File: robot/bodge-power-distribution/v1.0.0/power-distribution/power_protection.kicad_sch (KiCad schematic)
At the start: 34 parts

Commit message: Incomplete bodge-power-distribution schematics
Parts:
- removed R?: 10k, Resistor_SMD:R_0402_1005Metric_Pad0.72x0.64mm_HandSolder, symbol Device:R_Small_US
- added F?: TBD_MASTER_FUSE, symbol Device:Fuse
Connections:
- net V_{BATT}: now also F?.1; no longer Q?.3 (D), R?.1, U?.1 (V_{in})
- net FAULT_{OD} renamed ~{FAULT}
- net TEMP_MON_{pwr}_1v25 renamed TEMP_MON_{PWR(1v25)}
- net TempMon_{pwr} renamed TempMon_{PWR}
- new net: F?.2, Q?.3 (D), R?.1, U?.1 (V_{IN})
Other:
- note added: "Up to 80V"
- note removed: "up to 80V"
- title: Motorboard -> Power Distribution

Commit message: Incomplete bodge-power-distribution schematics
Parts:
- removed Q? (x2): SQJA80EP-T1_GE3, Package_TO_SOT_SMD:Vishay_PowerPAK_SC70-6L_Single, symbol Device:Q_NMOS_SGD
- removed R?: 69.8k, Resistor_SMD:R_0402_1005Metric_Pad0.72x0.64mm_HandSolder, symbol Device:R_Small_US
- removed R?: 115k, Resistor_SMD:R_0402_1005Metric_Pad0.72x0.64mm_HandSolder, symbol Device:R_Small_US
- added Q1, Q2: SQJA80EP-T1_GE3, Package_SO:PowerPAK_SO-8_Single, symbol transistors:Q_NMOS_SGD_PowerPAK
- added R4, R5: 39k, Resistor_SMD:R_0402_1005Metric_Pad0.72x0.64mm_HandSolder, symbol Device:R_Small_US
- gave numbers to parts that had none: 30
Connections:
- net GND: now also R4.2, R5.2
- net V_{BATT(PROTECTED)}: now also Q2.5 (D)
- net at F1.2, R6.1, U2.1 (V_{IN}): now also Q1.5 (D)
- net at R20.1: now also Q1.4 (G)
- net at U1.7 (CH6): now also R5.1
- net at U1.8 (CH7): now also R4.1
- net at R23.2: now also Q2.4 (G)
- new net: Q1.1 (S), Q1.2 (S), Q1.3 (S), Q2.1 (S), Q2.2 (S), Q2.3 (S)
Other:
- note added: "80V Tolerant"
- note removed: "Power Regulator Temperature Monitor Voltage Divider"
- note removed: "Up to 80V"
- moved on the sheet: C4, C5, C6, C7, F1, R10, R11, R12, R13, R14, R15, R16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

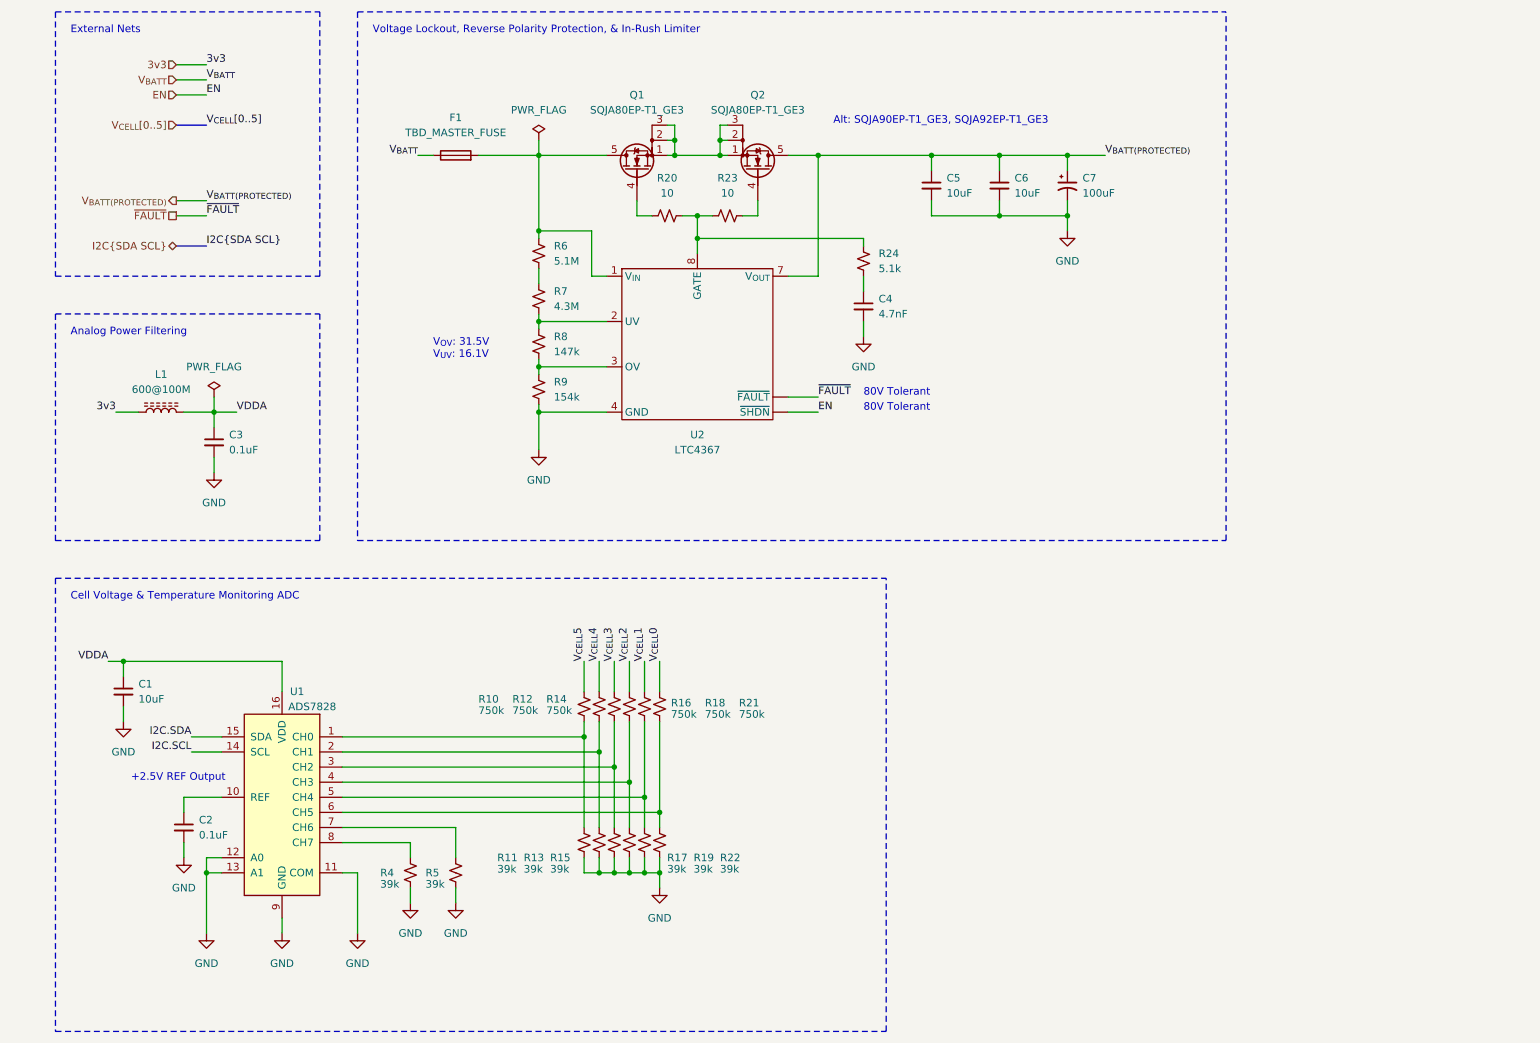
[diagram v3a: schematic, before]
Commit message: Separated power monitor into its own sheet
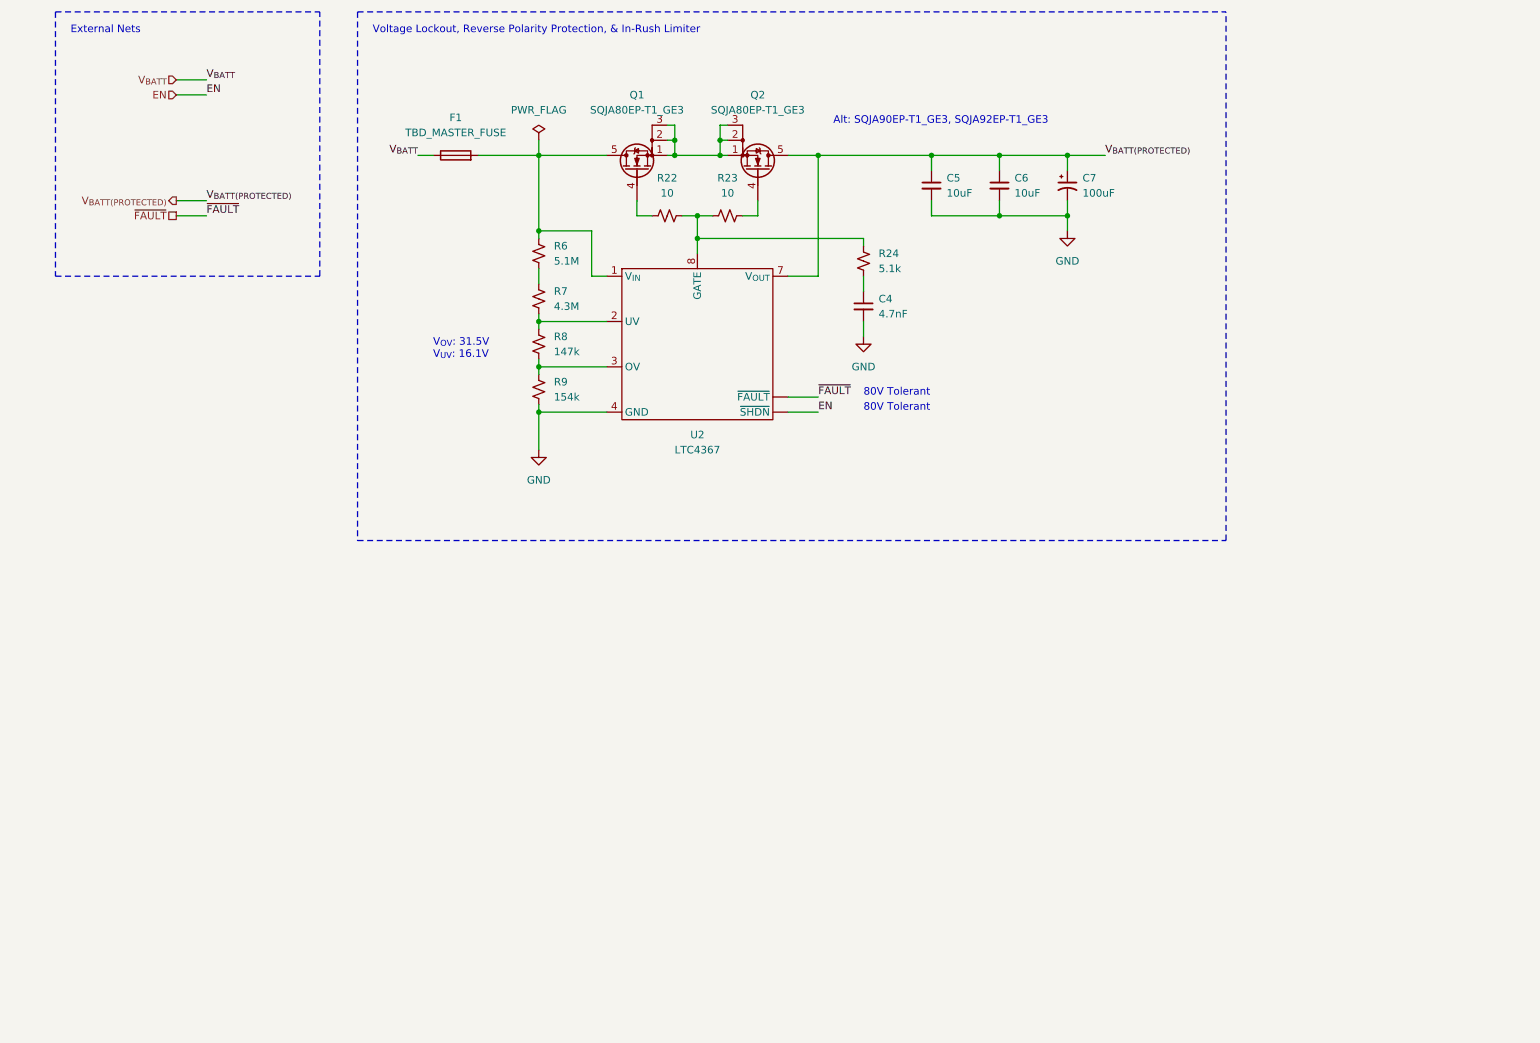
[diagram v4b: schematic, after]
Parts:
- removed C1: 10uF, Capacitor_SMD:C_1210_3225Metric_Pad1.33x2.70mm_HandSolder, symbol Device:C_Small
- removed C2, C3: 0.1uF, Capacitor_SMD:C_0402_1005Metric_Pad0.74x0.62mm_HandSolder, symbol Device:C_Small
- removed L1: 600@100M, Inductor_SMD:L_0603_1608Metric_Pad1.05x0.95mm_HandSolder, symbol Device:L_Ferrite
- removed R10, R12, R14, R16, R18, R21: 750k, Resistor_SMD:R_0402_1005Metric_Pad0.72x0.64mm_HandSolder, symbol Device:R_Small_US
- removed R11, R13, R15, R17, R19, R22, R4, R5: 39k, Resistor_SMD:R_0402_1005Metric_Pad0.72x0.64mm_HandSolder, symbol Device:R_Small_US
- removed U1: ADS7828, Package_SO:TSSOP-16_4.4x5mm_P0.65mm, symbol Analog_ADC:ADS7828
- renumbered R20 to R22
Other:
- note removed: "+2.5V REF Output"
- note removed: "Analog Power Filtering"
- note removed: "Cell Voltage & Temperature Monitoring ADC"

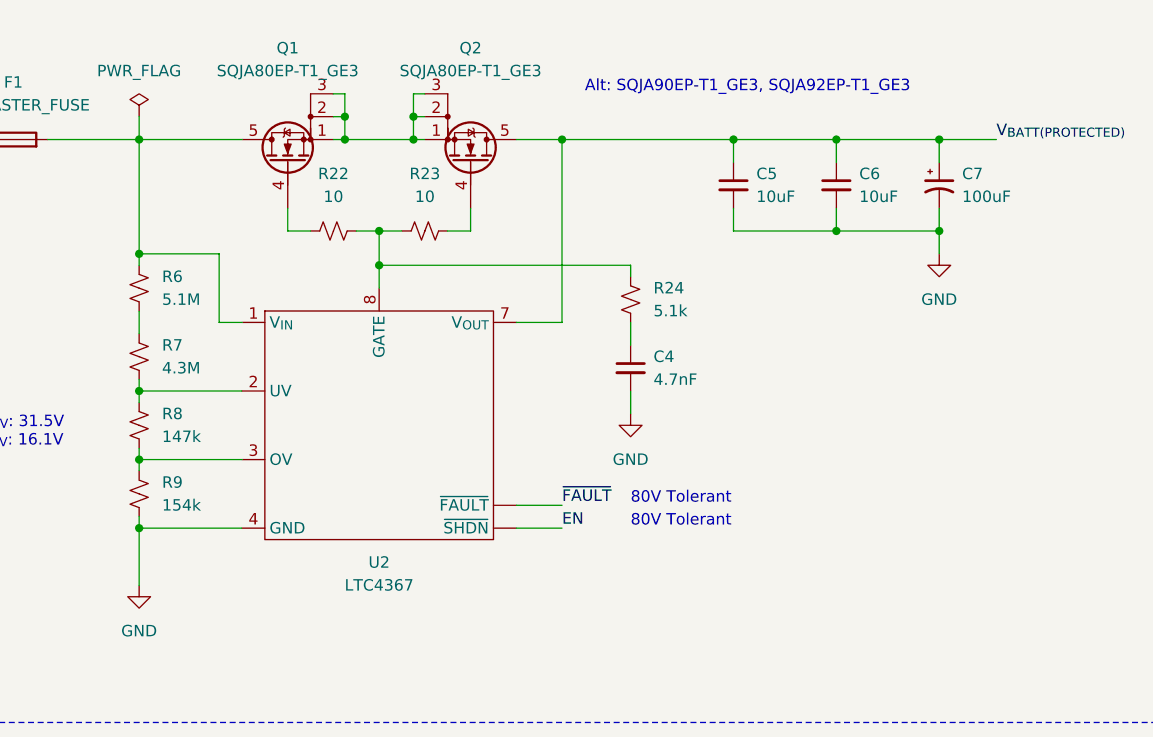
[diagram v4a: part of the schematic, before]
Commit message: Rename transistors library to AT-Transistors
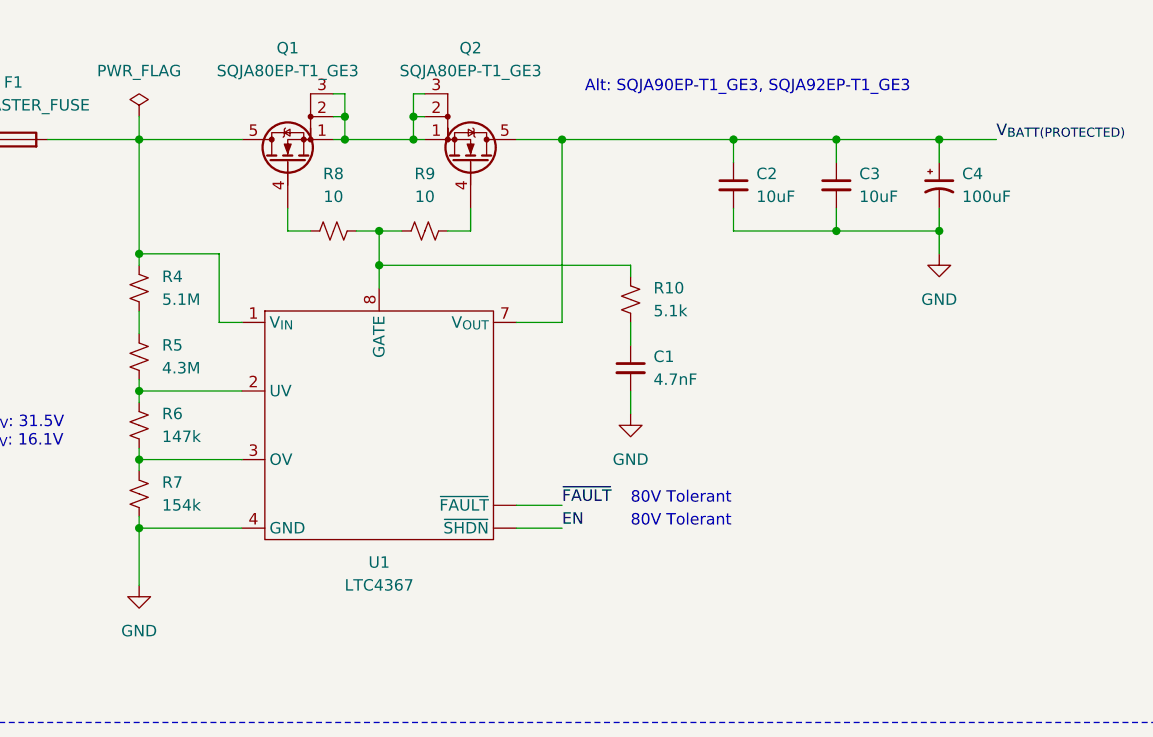
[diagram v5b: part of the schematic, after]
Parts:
- removed Q1: SQJA80EP-T1_GE3, Package_SO:PowerPAK_SO-8_Single, symbol transistors:Q_NMOS_SGD_PowerPAK
- added Q1: SQJA80EP-T1_GE3, Package_SO:PowerPAK_SO-8_Single, symbol AT-Transistors:Q_NMOS_SGD_PowerPAK
- Q2: symbol transistors:Q_NMOS_SGD_PowerPAK -> AT-Transistors:Q_NMOS_SGD_PowerPAK
- renumbered C4 to C1, C5 to C2, C6 to C3, C7 to C4, R24 to R10, R6 to R4, R7 to R5, R8 to R6, R9 to R7, R22 to R8, R23 to R9, U2 to U1
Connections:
- net at F1.2, R4.1, U1.1 (V_{IN}): now also Q1.5 (D)
- net at Q2.1 (S), Q2.2 (S), Q2.3 (S): now also Q1.1 (S), Q1.2 (S), Q1.3 (S)
- net at R8.1: now also Q1.4 (G)
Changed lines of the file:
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@@
   (symbol (lib_id "Device:R_Small_US") (at 100.33 59.69 0) (unit 1)
     (in_bom yes) (on_board yes) (fields_autoplaced)
-    (property "Reference" "R6" (id 0) (at 102.87 58.4199 0)
+    (property "Reference" "R4" (id 0) (at 102.87 58.4199 0)
       (effects (font (size 1.27 1.27)) (justify left))
     )
@@
     (pin "2")
   )
-  (symbol (lib_id "transistors:Q_NMOS_SGD_PowerPAK") (at 137.16 45.72 270) (mirror x) (unit 1)
+  (symbol (lib_id "AT-Transistors:Q_NMOS_SGD_PowerPAK") (at 137.16 45.72 270) (mirror x) (unit 1)
     (in_bom yes) (on_board yes)
     (property "Reference" "Q2" (id 0) (at 137.16 33.02 90))
@@
   (symbol (lib_id "Device:R_Small_US") (at 100.33 67.31 0) (unit 1)
     (in_bom yes) (on_board yes) (fields_autoplaced)
-    (property "Reference" "R7" (id 0) (at 102.87 66.0399 0)
+    (property "Reference" "R5" (id 0) (at 102.87 66.0399 0)
       (effects (font (size 1.27 1.27)) (justify left))
     )
@@
     (pin "2")
   )
+  (symbol (lib_id "AT-Transistors:Q_NMOS_SGD_PowerPAK") (at 116.84 45.72 90) (unit 1)
+    (in_bom yes) (on_board yes)
+    (property "Reference" "Q1" (id 0) (at 116.84 33.02 90))
+    (property "Value" "SQJA80EP-T1_GE3" (id 1) (at 116.84 35.56 90))
+    (property "Footprint" "Package_SO:PowerPAK_SO-8_Single" (id 2) (at 114.3 40.64 0)
+      (effects (font (size 1.27 1.27)) hide)
+    )
+    (property "Datasheet" "~" (id 3) (at 116.84 45.72 0)
+      (effects (font (size 1.27 1.27)) hide)
+    )
+    (pin "1")
+    (pin "2")
+    (pin "3")
+    (pin "4")
+    (pin "5")
+  )
   (symbol (lib_id "Device:C_Polarized_Small_US") (at 189.23 48.26 0) (unit 1)
     (in_bom yes) (on_board yes) (fields_autoplaced)
-    (property "Reference" "C7" (id 0) (at 191.77 46.9899 0)
+    (property "Reference" "C4" (id 0) (at 191.77 46.9899 0)
       (effects (font (size 1.27 1.27)) (justify left))
     )
@@
   (symbol (lib_id "Device:R_Small_US") (at 154.94 60.96 0) (unit 1)
     (in_bom yes) (on_board yes) (fields_autoplaced)
-    (property "Reference" "R24" (id 0) (at 157.48 59.6899 0)
+    (property "Reference" "R10" (id 0) (at 157.48 59.6899 0)
       (effects (font (size 1.27 1.27)) (justify left))
     )
@@
   (symbol (lib_id "power:GND") (at 154.94 73.66 0) (unit 1)
     (in_bom yes) (on_board yes) (fields_autoplaced)
-    (property "Reference" "#PWR022" (id 0) (at 154.94 80.01 0)
+    (property "Reference" "#PWR012" (id 0) (at 154.94 80.01 0)
       (effects (font (size 1.27 1.27)) hide)
     )
@@
   (symbol (lib_id "ltc_regulators:LTC4367") (at 127 74.93 0) (unit 1)
     (in_bom yes) (on_board yes) (fields_autoplaced)
-    (property "Reference" "U2" (id 0) (at 127 90.17 0))
+    (property "Reference" "U1" (id 0) (at 127 90.17 0))
     (property "Value" "LTC4367" (id 1) (at 127 92.71 0))
     (property "Footprint" "" (id 2) (at 127 74.93 0)
@@
   (symbol (lib_id "power:PWR_FLAG") (at 100.33 40.64 0) (unit 1)
     (in_bom yes) (on_board yes) (fields_autoplaced)
-    (property "Reference" "#FLG04" (id 0) (at 100.33 38.735 0)
+    (property "Reference" "#FLG03" (id 0) (at 100.33 38.735 0)
       (effects (font (size 1.27 1.27)) hide)
     )
@@
   (symbol (lib_id "power:GND") (at 189.23 55.88 0) (unit 1)
     (in_bom yes) (on_board yes) (fields_autoplaced)
-    (property "Reference" "#PWR023" (id 0) (at 189.23 62.23 0)
+    (property "Reference" "#PWR013" (id 0) (at 189.23 62.23 0)
       (effects (font (size 1.27 1.27)) hide)
     )
@@
   (symbol (lib_id "Device:C_Small") (at 166.37 48.26 0) (unit 1)
     (in_bom yes) (on_board yes) (fields_autoplaced)
-    (property "Reference" "C5" (id 0) (at 168.91 46.9899 0)
+    (property "Reference" "C2" (id 0) (at 168.91 46.9899 0)
       (effects (font (size 1.27 1.27)) (justify left))
     )
@@
   (symbol (lib_id "Device:C_Small") (at 177.8 48.26 0) (unit 1)
     (in_bom yes) (on_board yes) (fields_autoplaced)
-    (property "Reference" "C6" (id 0) (at 180.34 46.9899 0)
+    (property "Reference" "C3" (id 0) (at 180.34 46.9899 0)
       (effects (font (size 1.27 1.27)) (justify left))
     )
@@
   (symbol (lib_id "Device:R_Small_US") (at 132.08 53.34 90) (unit 1)
     (in_bom yes) (on_board yes) (fields_autoplaced)
-    (property "Reference" "R23" (id 0) (at 132.08 46.99 90))
+    (property "Reference" "R9" (id 0) (at 132.08 46.99 90))
     (property "Value" "10" (id 1) (at 132.08 49.53 90))
     (property "Footprint" "Resistor_SMD:R_0402_1005Metric_Pad0.72x0.64mm_HandSolder" (id 2) (at 132.08 53.34 0)
@@
   (symbol (lib_id "Device:C_Small") (at 154.94 68.58 0) (unit 1)
     (in_bom yes) (on_board yes) (fields_autoplaced)
-    (property "Reference" "C4" (id 0) (at 157.48 67.3099 0)
+    (property "Reference" "C1" (id 0) (at 157.48 67.3099 0)
       (effects (font (size 1.27 1.27)) (justify left))
     )
@@
   (symbol (lib_id "power:GND") (at 100.33 92.71 0) (unit 1)
     (in_bom yes) (on_board yes)
-    (property "Reference" "#PWR020" (id 0) (at 100.33 99.06 0)
+    (property "Reference" "#PWR011" (id 0) (at 100.33 99.06 0)
       (effects (font (size 1.27 1.27)) hide)
     )
@@
   (symbol (lib_id "Device:R_Small_US") (at 100.33 74.93 0) (unit 1)
     (in_bom yes) (on_board yes) (fields_autoplaced)
-    (property "Reference" "R8" (id 0) (at 102.87 73.6599 0)
+    (property "Reference" "R6" (id 0) (at 102.87 73.6599 0)
       (effects (font (size 1.27 1.27)) (justify left))
     )
@@
   (symbol (lib_id "Device:R_Small_US") (at 121.92 53.34 90) (unit 1)
     (in_bom yes) (on_board yes) (fields_autoplaced)
-    (property "Reference" "R22" (id 0) (at 121.92 46.99 90))
+    (property "Reference" "R8" (id 0) (at 121.92 46.99 90))
     (property "Value" "10" (id 1) (at 121.92 49.53 90))
     (property "Footprint" "Resistor_SMD:R_0402_1005Metric_Pad0.72x0.64mm_HandSolder" (id 2) (at 121.92 53.34 0)
@@
   (symbol (lib_id "Device:R_Small_US") (at 100.33 82.55 180) (unit 1)
     (in_bom yes) (on_board yes) (fields_autoplaced)
-    (property "Reference" "R9" (id 0) (at 102.87 81.2799 0)
+    (property "Reference" "R7" (id 0) (at 102.87 81.2799 0)
       (effects (font (size 1.27 1.27)) (justify right))
     )
@@
     (pin "2")
   )
-  (symbol (lib_id "transistors:Q_NMOS_SGD_PowerPAK") (at 116.84 45.72 90) (unit 1)
-    (in_bom yes) (on_board yes)
-    (property "Reference" "Q1" (id 0) (at 116.84 33.02 90))
-    (property "Value" "SQJA80EP-T1_GE3" (id 1) (at 116.84 35.56 90))
-    (property "Footprint" "Package_SO:PowerPAK_SO-8_Single" (id 2) (at 114.3 40.64 0)
-      (effects (font (size 1.27 1.27)) hide)
-    )
-    (property "Datasheet" "~" (id 3) (at 116.84 45.72 0)
-      (effects (font (size 1.27 1.27)) hide)
-    )
-    (pin "1")
-    (pin "2")
-    (pin "3")
-    (pin "4")
-    (pin "5")
-  )
 )

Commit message: Component updates
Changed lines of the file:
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@@
     (stroke (width 0) (type solid) (color 0 0 0 0))
   )
-  (wire (pts (xy 100.33 86.36) (xy 100.33 92.71))
+  (wire (pts (xy 100.33 86.36) (xy 100.33 87.63))
     (stroke (width 0) (type solid) (color 0 0 0 0))
   )
@@
     (pin "2")
   )
-  (symbol (lib_id "power:GND") (at 100.33 92.71 0) (unit 1)
+  (symbol (lib_id "power:GND") (at 100.33 87.63 0) (unit 1)
     (in_bom yes) (on_board yes)
-    (property "Reference" "#PWR011" (id 0) (at 100.33 99.06 0)
-      (effects (font (size 1.27 1.27)) hide)
-    )
-    (property "Value" "GND" (id 1) (at 100.33 97.79 0))
-    (property "Footprint" "" (id 2) (at 100.33 92.71 0)
-      (effects (font (size 1.27 1.27)) hide)
-    )
-    (property "Datasheet" "" (id 3) (at 100.33 92.71 0)
-      (effects (font (size 1.27 1.27)) hide)
-    )
+    (property "Reference" "#PWR011" (id 0) (at 100.33 93.98 0)
+      (effects (font (size 1.27 1.27)) hide)
+    )
+    (property "Value" "GND" (id 1) (at 100.33 92.71 0))
+    (property "Footprint" "" (id 2) (at 100.33 87.63 0)
+      (effects (font (size 1.27 1.27)) hide)
+    )
+    (property "Datasheet" "" (id 3) (at 100.33 87.63 0)
+      (effects (font (size 1.27 1.27)) hide)
+    )
